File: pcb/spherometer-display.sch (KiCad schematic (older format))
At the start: 12 parts, among them J1 Battery, J2 Indicator, J3 Display, Q1 NPN, Q2 NPN, SW1 SmallPush, SW2 LargePush, U1 ATTINY85V-10SU

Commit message: Adapt to Kicad 5.1 symbols.
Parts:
- removed J3: Display, Pin_Headers:Pin_Header_Straight_1x04_Pitch2.54mm, symbol Connector:Conn_01x04
- removed SW1: SmallPush, Buttons_Switches_SMD:SW_SPST_PTS645, symbol Switch:SW_Push
- added J3: Display, Connector_PinHeader_2.54mm:PinHeader_1x04_P2.54mm_Vertical, symbol Connector_Generic:Conn_01x04
- C1: footprint Capacitors_SMD:C_0603 -> Capacitor_SMD:C_0603_1608Metric; symbol device:C -> Device:C
- J1: footprint Connectors_JST:JST_PH_S3B-PH-K_03x2.00mm_Angled -> Connector_JST:JST_PH_S3B-PH-K_1x03_P2.00mm_Horizontal; symbol Connector:Conn_01x03 -> Connector_Generic:Conn_01x03
- J2: footprint Connectors_JST:JST_PH_S4B-PH-K_04x2.00mm_Angled -> Connector_JST:JST_PH_S4B-PH-K_1x04_P2.00mm_Horizontal; symbol Connector:Conn_01x04 -> Connector_Generic:Conn_01x04
- Q1, Q2: footprint TO_SOT_Packages_SMD:SOT-23 -> Package_TO_SOT_SMD:SOT-23; symbol device:Q_NPN_BEC -> Device:Q_NPN_BEC
- R1, R2, R3: footprint Resistors_SMD:R_0603 -> Resistor_SMD:R_0603_1608Metric; symbol device:R -> Device:R
- SW2: value LargePush -> UI-Button; footprint Buttons_Switches_SMD:SW_SPST_TL3342 -> Button_Switch_THT:SW_Tactile_SPST_Angled_PTS645Vx83-2LFS
- U1: footprint Housings_SOIC:SOIC-8_3.9x4.9mm_Pitch1.27mm -> Package_SO:SOIC-8_3.9x4.9mm_P1.27mm; symbol atmel:ATTINY85-20SU -> MCU_Microchip_ATtiny:ATtiny85V-10SU
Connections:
- net GND: now also J3.3 (Pin_3)
- net SCL: now also J3.2 (Pin_2)
- net SDA: now also J3.1 (Pin_1)
- net VCC: now also J3.4 (Pin_4)
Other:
- note removed: "Alternatives"
- moved on the sheet: C1, R3, U1
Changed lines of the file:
@@
 $EndDescr
 $Comp
-L device:Q_NPN_BEC Q2
+L Device:Q_NPN_BEC Q2
 U 1 1 5C7BA6FA
 P 2750 4050
 F 0 "Q2" H 2941 4096 50  0000 L CNN
 F 1 "NPN" H 2941 4005 50  0000 L CNN
-F 2 "TO_SOT_Packages_SMD:SOT-23" H 2950 4150 50  0001 C CNN
+F 2 "Package_TO_SOT_SMD:SOT-23" H 2950 4150 50  0001 C CNN
 F 3 "" H 2750 4050 50  0001 C CNN
 	1    2750 4050
@@
 L power:VCC #PWR0103
 U 1 1 5C7BC608
-P 6100 2900
-F 0 "#PWR0103" H 6100 2750 50  0001 C CNN
-F 1 "VCC" H 6117 3073 50  0000 C CNN
-F 2 "" H 6100 2900 50  0001 C CNN
-F 3 "" H 6100 2900 50  0001 C CNN
-	1    6100 2900
+P 4950 2600
+F 0 "#PWR0103" H 4950 2450 50  0001 C CNN
+F 1 "VCC" H 4967 2773 50  0000 C CNN
+F 2 "" H 4950 2600 50  0001 C CNN
+F 3 "" H 4950 2600 50  0001 C CNN
+	1    4950 2600
 	1    0    0    -1
 $EndComp
@@
 L power:GND #PWR0104
 U 1 1 5C7BCED2
-P 6100 3400
-F 0 "#PWR0104" H 6100 3150 50  0001 C CNN
-F 1 "GND" H 6105 3227 50  0000 C CNN
-F 2 "" H 6100 3400 50  0001 C CNN
-F 3 "" H 6100 3400 50  0001 C CNN
-	1    6100 3400
-	1    0    0    -1
-$EndComp
-$Comp
-L Connector:Conn_01x04 J3
-U 1 1 5C7BD895
-P 2750 2200
-F 0 "J3" V 2714 1912 50  0000 R CNN
-F 1 "Display" V 2623 1912 50  0000 R CNN
-F 2 "Pin_Headers:Pin_Header_Straight_1x04_Pitch2.54mm" H 2750 2200 50  0001 C CNN
-F 3 "~" H 2750 2200 50  0001 C CNN
-	1    2750 2200
-	0    -1   -1   0
+P 4950 3800
+F 0 "#PWR0104" H 4950 3550 50  0001 C CNN
+F 1 "GND" H 4955 3627 50  0000 C CNN
+F 2 "" H 4950 3800 50  0001 C CNN
+F 3 "" H 4950 3800 50  0001 C CNN
+	1    4950 3800
+	1    0    0    -1
 $EndComp
 $Comp
@@
 $EndComp
 $Comp
-L atmel:ATTINY85-20SU U1
+L MCU_Microchip_ATtiny:ATtiny85V-10SU U1
 U 1 1 5C7C0CD1
-P 4750 3150
-F 0 "U1" H 4750 3667 50  0000 C CNN
-F 1 "ATTINY85V-10SU" H 4750 3576 50  0000 C CNN
-F 2 "Housings_SOIC:SOIC-8_3.9x4.9mm_Pitch1.27mm" H 5700 3150 50  0001 C CIN
-F 3 "http://www.atmel.com/images/atmel-2586-avr-8-bit-microcontroller-attiny25-attiny45-attiny85_datasheet.pdf" H 4750 3150 50  0001 C CNN
-	1    4750 3150
-	1    0    0    -1
+P 4050 3200
+F 0 "U1" H 3650 3450 50  0000 C CNN
+F 1 "ATTINY85V-10SU" H 3900 3350 50  0000 C CNN
+F 2 "Package_SO:SOIC-8_3.9x4.9mm_P1.27mm" H 5000 3200 50  0001 C CIN
+F 3 "http://www.atmel.com/images/atmel-2586-avr-8-bit-microcontroller-attiny25-attiny45-attiny85_datasheet.pdf" H 4050 3200 50  0001 C CNN
+	1    4050 3200
+	-1   0    0    -1
 $EndComp
 Wire Wire Line
 	2650 2400 2650 2900
 Wire Wire Line
-	2650 2900 3400 2900
+	2650 2900 3450 2900
 Wire Wire Line
 	2750 2400 2750 3100
 Wire Wire Line
-	2750 3100 3400 3100
+	2750 3100 3450 3100
 Text Label 2900 2900 0    50   ~ 0
 SDA
@@
 P 3750 2400
 F 0 "SW2" H 4250 2500 50  0000 C CNN
-F 1 "LargePush" H 4250 2400 50  0000 C CNN
-F 2 "Buttons_Switches_SMD:SW_SPST_TL3342" H 3750 2600 50  0001 C CNN
+F 1 "UI-Button" H 4250 2400 50  0000 C CNN
+F 2 "Button_Switch_THT:SW_Tactile_SPST_Angled_PTS645Vx83-2LFS" H 3750 2600 50  0001 C CNN
 F 3 "" H 3750 2600 50  0001 C CNN
 	1    3750 2400
@@
 	3300 2400 3300 3000
 Wire Wire Line
-	3300 3000 3400 3000
+	3300 3000 3450 3000
 Text Label 3300 2600 0    50   ~ 0
 Button
 Wire Wire Line
-	2850 3200 3400 3200
+	2850 3200 3450 3200
 Wire Wire Line
 	2850 3850 3200 3850
@@
 	3200 3850 3200 3300
 Wire Wire Line
-	3200 3300 3400 3300
-$Comp
-L device:Q_NPN_BEC Q1
+	3200 3300 3450 3300
+$Comp
+L Device:Q_NPN_BEC Q1
 U 1 1 5C7C80D0
 P 2750 3400
 F 0 "Q1" H 2941 3446 50  0000 L CNN
 F 1 "NPN" H 2941 3355 50  0000 L CNN
-F 2 "TO_SOT_Packages_SMD:SOT-23" H 2950 3500 50  0001 C CNN
+F 2 "Package_TO_SOT_SMD:SOT-23" H 2950 3500 50  0001 C CNN
 F 3 "" H 2750 3400 50  0001 C CNN
 	1    2750 3400
@@
 $EndComp
 $Comp
-L Connector:Conn_01x04 J2
+L Connector_Generic:Conn_01x04 J2
 U 1 1 5C7C8F49
 P 2050 2200
-F 0 "J2" V 2014 1912 50  0000 R CNN
+F 0 "J2" V 2050 2450 50  0000 R CNN
 F 1 "Indicator" V 1950 2700 50  0000 R CNN
-F 2 "Connectors_JST:JST_PH_S4B-PH-K_04x2.00mm_Angled" H 2050 2200 50  0001 C CNN
+F 2 "Connector_JST:JST_PH_S4B-PH-K_1x04_P2.00mm_Horizontal" H 2050 2200 50  0001 C CNN
 F 3 "~" H 2050 2200 50  0001 C CNN
 	1    2050 2200
@@
 $EndComp
 $Comp
-L device:R R1
+L Device:R R1
 U 1 1 5C7CA7C5
 P 2400 3400
 F 0 "R1" V 2193 3400 50  0000 C CNN
 F 1 "33k" V 2284 3400 50  0000 C CNN
-F 2 "Resistors_SMD:R_0603" V 2330 3400 50  0001 C CNN
+F 2 "Resistor_SMD:R_0603_1608Metric" V 2330 3400 50  0001 C CNN
 F 3 "" H 2400 3400 50  0001 C CNN
 	1    2400 3400
@@
 $EndComp
 $Comp
-L device:R R2
+L Device:R R2
 U 1 1 5C7CB12C
 P 2400 4050
 F 0 "R2" V 2193 4050 50  0000 C CNN
 F 1 "33k" V 2284 4050 50  0000 C CNN
-F 2 "Resistors_SMD:R_0603" V 2330 4050 50  0001 C CNN
+F 2 "Resistor_SMD:R_0603_1608Metric" V 2330 4050 50  0001 C CNN
 F 3 "" H 2400 4050 50  0001 C CNN
 	1    2400 4050
@@
 	2050 4050 2250 4050
 $Comp
-L Connector:Conn_01x03 J1
+L Connector_Generic:Conn_01x03 J1
 U 1 1 5C7CC029
 P 1300 3050
 F 0 "J1" H 1300 2850 50  0000 C CNN
 F 1 "Battery" H 1500 3050 50  0000 C CNN
-F 2 "Connectors_JST:JST_PH_S3B-PH-K_03x2.00mm_Angled" H 1300 3050 50  0001 C CNN
+F 2 "Connector_JST:JST_PH_S3B-PH-K_1x03_P2.00mm_Horizontal" H 1300 3050 50  0001 C CNN
 F 3 "~" H 1300 3050 50  0001 C CNN
 	1    1300 3050
@@
 $EndComp
 $Comp
-L Switch:SW_Push SW1
-U 1 1 5C7D1A93
-P 3750 2200
-F 0 "SW1" H 4200 2300 50  0000 C CNN
-F 1 "SmallPush" H 4250 2200 50  0000 C CNN
-F 2 "Buttons_Switches_SMD:SW_SPST_PTS645" H 3750 2400 50  0001 C CNN
-F 3 "" H 3750 2400 50  0001 C CNN
-	1    3750 2200
-	1    0    0    -1
-$EndComp
-Wire Wire Line
-	3550 2200 3550 2400
-Connection ~ 3550 2400
-Wire Wire Line
-	3950 2200 3950 2400
-Connection ~ 3950 2400
-Text Notes 4500 2350 0    50   ~ 0
-Alternatives
-$Comp
-L device:R R3
+L Device:R R3
 U 1 1 5C7D3C7F
-P 3400 3550
-F 0 "R3" H 3330 3504 50  0000 R CNN
-F 1 "33k" H 3330 3595 50  0000 R CNN
-F 2 "Resistors_SMD:R_0603" V 3330 3550 50  0001 C CNN
-F 3 "" H 3400 3550 50  0001 C CNN
-	1    3400 3550
+P 3350 3550
+F 0 "R3" H 3300 3700 50  0000 R CNN
+F 1 "33k" V 3350 3650 50  0000 R CNN
+F 2 "Resistor_SMD:R_0603_1608Metric" V 3280 3550 50  0001 C CNN
+F 3 "" H 3350 3550 50  0001 C CNN
+	1    3350 3550
 	-1   0    0    1
 $EndComp
@@
 L power:VCC #PWR01
 U 1 1 5C7D4897
-P 3400 3700
-F 0 "#PWR01" H 3400 3550 50  0001 C CNN
-F 1 "VCC" V 3417 3828 50  0000 L CNN
-F 2 "" H 3400 3700 50  0001 C CNN
-F 3 "" H 3400 3700 50  0001 C CNN
-	1    3400 3700
-	0    1    1    0
-$EndComp
-$Comp
-L device:C C1
+P 3350 3700
+F 0 "#PWR01" H 3350 3550 50  0001 C CNN
+F 1 "VCC" V 3367 3828 50  0000 L CNN
+F 2 "" H 3350 3700 50  0001 C CNN
+F 3 "" H 3350 3700 50  0001 C CNN
+	1    3350 3700
+	-1   0    0    1
+$EndComp
+$Comp
+L Device:C C1
 U 1 1 5C7B9330
-P 6100 3150
-F 0 "C1" H 6215 3196 50  0000 L CNN
-F 1 "100n" H 6215 3105 50  0000 L CNN
-F 2 "Capacitors_SMD:C_0603" H 6138 3000 50  0001 C CNN
-F 3 "" H 6100 3150 50  0001 C CNN
-	1    6100 3150
-	1    0    0    -1
-$EndComp
-Wire Wire Line
-	6100 2900 6100 3000
-Connection ~ 6100 2900
-Wire Wire Line
-	6100 3300 6100 3400
-Connection ~ 6100 3400
+P 4950 3200
+F 0 "C1" H 5065 3246 50  0000 L CNN
+F 1 "100n" H 5065 3155 50  0000 L CNN
+F 2 "Capacitor_SMD:C_0603_1608Metric" H 4988 3050 50  0001 C CNN
+F 3 "" H 4950 3200 50  0001 C CNN
+	1    4950 3200
+	1    0    0    -1
+$EndComp
+$Comp
+L Connector_Generic:Conn_01x04 J3
+U 1 1 5CBCFE92
+P 2750 2200
+F 0 "J3" V 2714 1912 50  0000 R CNN
+F 1 "Display" V 2650 1950 50  0000 R CNN
+F 2 "Connector_PinHeader_2.54mm:PinHeader_1x04_P2.54mm_Vertical" H 2750 2200 50  0001 C CNN
+F 3 "~" H 2750 2200 50  0001 C CNN
+	1    2750 2200
+	0    -1   -1   0
+$EndComp
+Wire Wire Line
+	3450 3400 3350 3400
+Wire Wire Line
+	4050 3800 4950 3800
+Wire Wire Line
+	4950 3350 4950 3800
+Connection ~ 4950 3800
+Wire Wire Line
+	4050 2600 4950 2600
+Wire Wire Line
+	4950 2600 4950 3050
+Connection ~ 4950 2600
 $EndSCHEMATC

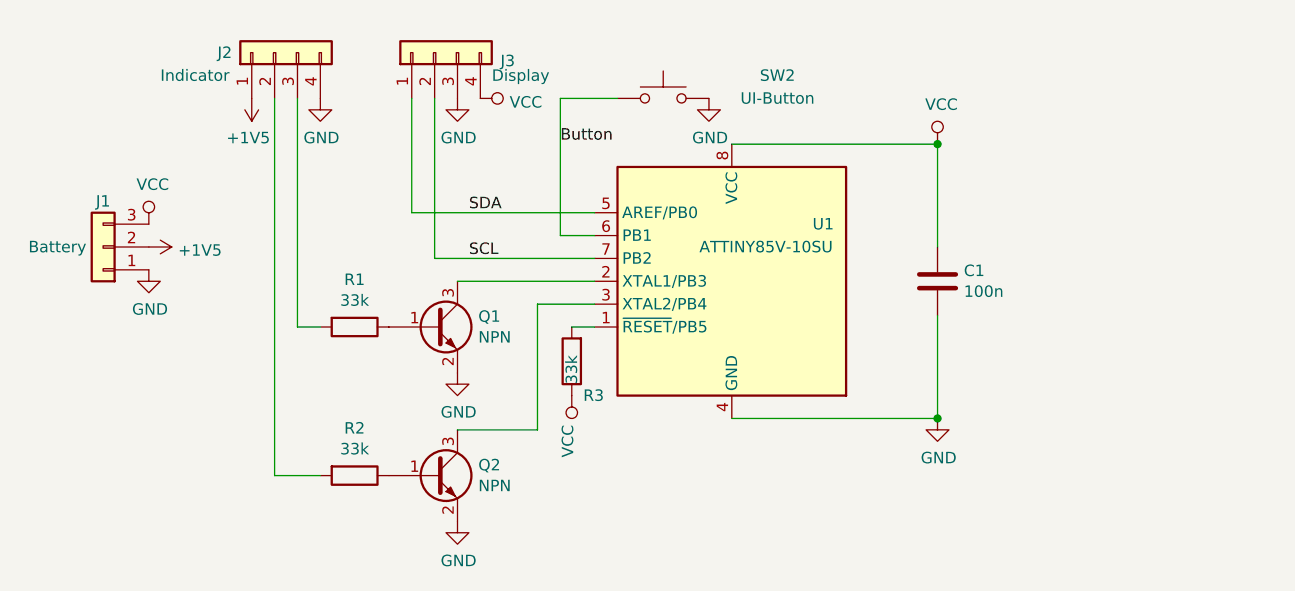
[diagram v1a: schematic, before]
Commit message: Prepare to be usable with dial indicators that already provide OpenCollector output.
Add a solder-jumper that allows to directly wire the indicator directly to Attiny.
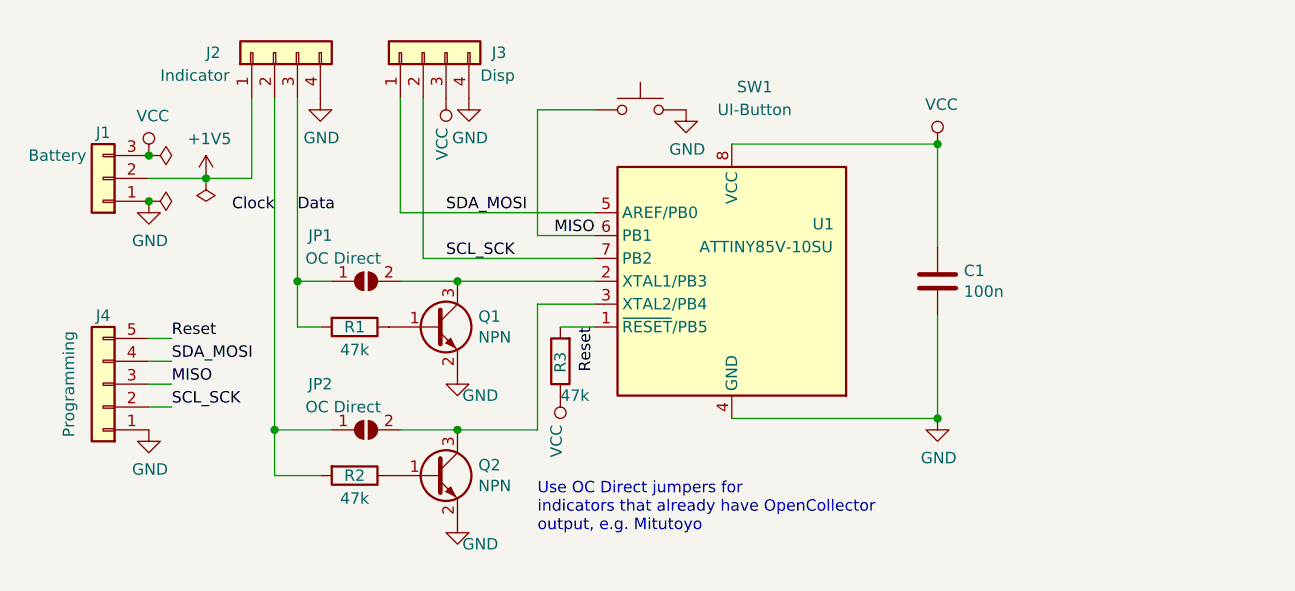
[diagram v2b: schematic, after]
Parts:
- added J4: Programming, Connector_PinHeader_2.54mm:PinHeader_1x05_P2.54mm_Vertical, symbol Connector_Generic:Conn_01x05
- added JP1, JP2: OC Direct, Jumper:SolderJumper-2_P1.3mm_Open_RoundedPad1.0x1.5mm, symbol Jumper:SolderJumper_2_Open
- J3: value Display -> Disp
- R1, R2, R3: value 33k -> 47k
- SW1: renamed from SW2; footprint Button_Switch_THT:SW_Tactile_SPST_Angled_PTS645Vx83-2LFS -> digi-spherometer:EVPAV-Switch
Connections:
- net GND: now also J3.4 (Pin_4), J4.1 (Pin_1); no longer J3.3 (Pin_3)
- net VCC: now also J3.3 (Pin_3); no longer J3.4 (Pin_4)
- net at Q2.3 (C), U1.3 (XTAL2/PB4): now also JP2.2 (B)
- net Reset: now reaches R3.2, U1.1 (~RESET~/PB5)
- net Reset: now also J4.5 (Pin_5)
- net at Q1.3 (C), U1.2 (XTAL1/PB3): now also JP1.2 (B)
- net Clock: now reaches J2.2 (Pin_2), R2.2
- net Clock: now also JP2.1 (A)
- net Data: now reaches J2.3 (Pin_3), R1.2
- net Data: now also JP1.1 (A)
- net Button renamed MISO
- net MISO: now also J4.3 (Pin_3)
- net SCL renamed SCL_SCK
- net SCL_SCK: now also J4.2 (Pin_2)
- net SDA renamed SDA_MOSI
- net SDA_MOSI: now also J4.4 (Pin_4)
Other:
- note added: "Use OC Direct jumpers for\nindicators that already have OpenCollector\noutput, e.g. Mitutoyo"
- moved on the sheet: J1, J3, R3, SW1

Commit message: Route board; add Makefile to create fab files.
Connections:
- net GND: now also SW1.1; no longer SW1.2
- net MISO: now also SW1.2; no longer SW1.1
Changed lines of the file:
@@
 U 1 1 5C7C2518
 P 3650 2450
-F 0 "SW1" H 4150 2550 50  0000 C CNN
-F 1 "UI-Button" H 4150 2450 50  0000 C CNN
+F 0 "SW1" H 3450 2600 50  0000 C CNN
+F 1 "UI-Button" H 3300 2500 50  0000 C CNN
 F 2 "digi-spherometer:EVPAV-Switch" H 3650 2650 50  0001 C CNN
 F 3 "" H 3650 2650 50  0001 C CNN
 	1    3650 2450
-	1    0    0    -1
+	-1   0    0    -1
 $EndComp
 $Comp

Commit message: Swap pin sequence of indicator connector.
With a flat cable from the autolet indicator, the GND pin is towards
the center.
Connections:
- net +1V5: now also J2.4 (Pin_4); no longer J2.1 (Pin_1)
- net Clock: now also J2.3 (Pin_3), JP1.1 (A), R1.2; no longer J2.2 (Pin_2), JP2.1 (A), R2.2
- net Data: now also J2.2 (Pin_2), JP2.1 (A), R2.2; no longer J2.3 (Pin_3), JP1.1 (A), R1.2
- net GND: now also J2.1 (Pin_1), J3.1 (Pin_1); no longer J2.4 (Pin_4), J3.4 (Pin_4)
- net SCL_SCK: now also J3.3 (Pin_3); no longer J3.2 (Pin_2)
- net SDA_MOSI: now also J3.4 (Pin_4); no longer J3.1 (Pin_1)
- net VCC: now also J3.2 (Pin_2); no longer J3.3 (Pin_3)
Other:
- note added: "Use OC Direct jumpers for\nindicators that already have OpenCollector\noutput, e.g. Mitutoyo\nThen R1, R2, Q1, Q2 are not needed."
- note removed: "Use OC Direct jumpers for\nindicators that already have OpenCollector\noutput, e.g. Mitutoyo"
- moved on the sheet: JP1, JP2, Q1, Q2, R1, R2
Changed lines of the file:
@@
 L Device:Q_NPN_BEC Q2
 U 1 1 5C7BA6FA
-P 2750 4050
-F 0 "Q2" H 2941 4096 50  0000 L CNN
-F 1 "NPN" H 2941 4005 50  0000 L CNN
-F 2 "Package_TO_SOT_SMD:SOT-23" H 2950 4150 50  0001 C CNN
-F 3 "" H 2750 4050 50  0001 C CNN
-	1    2750 4050
+P 2750 3400
+F 0 "Q2" H 2941 3446 50  0000 L CNN
+F 1 "NPN" H 2941 3355 50  0000 L CNN
+F 2 "Package_TO_SOT_SMD:SOT-23" H 2950 3500 50  0001 C CNN
+F 3 "" H 2750 3400 50  0001 C CNN
+	1    2750 3400
 	1    0    0    -1
 $EndComp
@@
 $EndComp
 Wire Wire Line
-	2850 3200 3450 3200
-Wire Wire Line
 	2850 3850 3200 3850
-Wire Wire Line
-	3200 3850 3200 3300
-Wire Wire Line
-	3200 3300 3450 3300
 $Comp
 L Device:Q_NPN_BEC Q1
 U 1 1 5C7C80D0
-P 2750 3400
-F 0 "Q1" H 2941 3446 50  0000 L CNN
-F 1 "NPN" H 2941 3355 50  0000 L CNN
-F 2 "Package_TO_SOT_SMD:SOT-23" H 2950 3500 50  0001 C CNN
-F 3 "" H 2750 3400 50  0001 C CNN
-	1    2750 3400
+P 2750 4050
+F 0 "Q1" H 2941 4096 50  0000 L CNN
+F 1 "NPN" H 2941 4005 50  0000 L CNN
+F 2 "Package_TO_SOT_SMD:SOT-23" H 2950 4150 50  0001 C CNN
+F 3 "" H 2750 4050 50  0001 C CNN
+	1    2750 4050
 	1    0    0    -1
 $EndComp
@@
 L Connector_Generic:Conn_01x04 J2
 U 1 1 5C7C8F49
-P 2050 2200
-F 0 "J2" V 2050 2500 50  0000 R CNN
-F 1 "Indicator" V 1950 2700 50  0000 R CNN
-F 2 "Connector_JST:JST_PH_S4B-PH-K_1x04_P2.00mm_Horizontal" H 2050 2200 50  0001 C CNN
-F 3 "~" H 2050 2200 50  0001 C CNN
-	1    2050 2200
-	0    -1   -1   0
+P 2150 2200
+F 0 "J2" V 2150 1900 50  0000 R CNN
+F 1 "Indicator" V 2050 1900 50  0000 R CNN
+F 2 "Connector_JST:JST_PH_S4B-PH-K_1x04_P2.00mm_Horizontal" H 2150 2200 50  0001 C CNN
+F 3 "~" H 2150 2200 50  0001 C CNN
+	1    2150 2200
+	0    1    -1   0
 $EndComp
 $Comp
@@
 L Device:R R1
 U 1 1 5C7CA7C5
+P 2400 4050
+F 0 "R1" V 2400 4050 50  0000 C CNN
+F 1 "47k" V 2500 4050 50  0000 C CNN
+F 2 "Resistor_SMD:R_0603_1608Metric" V 2330 4050 50  0001 C CNN
+F 3 "" H 2400 4050 50  0001 C CNN
+	1    2400 4050
+	0    1    1    0
+$EndComp
+$Comp
+L Device:R R2
+U 1 1 5C7CB12C
 P 2400 3400
-F 0 "R1" V 2400 3400 50  0000 C CNN
+F 0 "R2" V 2400 3400 50  0000 C CNN
 F 1 "47k" V 2500 3400 50  0000 C CNN
 F 2 "Resistor_SMD:R_0603_1608Metric" V 2330 3400 50  0001 C CNN
 F 3 "" H 2400 3400 50  0001 C CNN
 	1    2400 3400
-	0    1    1    0
-$EndComp
-$Comp
-L Device:R R2
-U 1 1 5C7CB12C
-P 2400 4050
-F 0 "R2" V 2400 4050 50  0000 C CNN
-F 1 "47k" V 2500 4050 50  0000 C CNN
-F 2 "Resistor_SMD:R_0603_1608Metric" V 2330 4050 50  0001 C CNN
-F 3 "" H 2400 4050 50  0001 C CNN
-	1    2400 4050
 	0    1    1    0
 $EndComp
@@
 L Connector_Generic:Conn_01x04 J3
 U 1 1 5CBCFE92
-P 2700 2200
-F 0 "J3" V 2700 1900 50  0000 R CNN
-F 1 "Disp" V 2600 1950 50  0000 R CNN
-F 2 "Connector_PinHeader_2.54mm:PinHeader_1x04_P2.54mm_Vertical" H 2700 2200 50  0001 C CNN
-F 3 "~" H 2700 2200 50  0001 C CNN
-	1    2700 2200
-	0    -1   -1   0
+P 2800 2200
+F 0 "J3" V 2800 2500 50  0000 R CNN
+F 1 "Disp" V 2700 2550 50  0000 R CNN
+F 2 "Connector_PinHeader_2.54mm:PinHeader_1x04_P2.54mm_Vertical" H 2800 2200 50  0001 C CNN
+F 3 "~" H 2800 2200 50  0001 C CNN
+	1    2800 2200
+	0    1    -1   0
 $EndComp
 Wire Wire Line
@@
 L Jumper:SolderJumper_2_Open JP1
 U 1 1 5CC4FCB3
+P 2450 3850
+F 0 "JP1" H 2250 4050 50  0000 C CNN
+F 1 "OC Direct" H 2350 3950 50  0000 C CNN
+F 2 "Jumper:SolderJumper-2_P1.3mm_Open_RoundedPad1.0x1.5mm" H 2450 3850 50  0001 C CNN
+F 3 "~" H 2450 3850 50  0001 C CNN
+	1    2450 3850
+	1    0    0    -1
+$EndComp
+Wire Wire Line
+	2150 3200 2300 3200
+Connection ~ 2150 3200
+Wire Wire Line
+	2150 3200 2150 3400
+Wire Wire Line
+	2600 3200 2850 3200
+$Comp
+L Jumper:SolderJumper_2_Open JP2
+U 1 1 5CC51175
 P 2450 3200
-F 0 "JP1" H 2250 3400 50  0000 C CNN
+F 0 "JP2" H 2250 3400 50  0000 C CNN
 F 1 "OC Direct" H 2350 3300 50  0000 C CNN
 F 2 "Jumper:SolderJumper-2_P1.3mm_Open_RoundedPad1.0x1.5mm" H 2450 3200 50  0001 C CNN
 F 3 "~" H 2450 3200 50  0001 C CNN
 	1    2450 3200
-	1    0    0    -1
-$EndComp
-Wire Wire Line
-	2150 3200 2300 3200
-Connection ~ 2150 3200
-Wire Wire Line
-	2150 3200 2150 3400
-Wire Wire Line
-	2600 3200 2850 3200
-Connection ~ 2850 3200
-$Comp
-L Jumper:SolderJumper_2_Open JP2
-U 1 1 5CC51175
-P 2450 3850
-F 0 "JP2" H 2250 4050 50  0000 C CNN
-F 1 "OC Direct" H 2350 3950 50  0000 C CNN
-F 2 "Jumper:SolderJumper-2_P1.3mm_Open_RoundedPad1.0x1.5mm" H 2450 3850 50  0001 C CNN
-F 3 "~" H 2450 3850 50  0001 C CNN
-	1    2450 3850
 	1    0    0    -1
 $EndComp
@@
 Wire Wire Line
 	3200 3000 3450 3000
-Text Notes 3200 4300 0    50   ~ 0
-Use OC Direct jumpers for\nindicators that already have OpenCollector\noutput, e.g. Mitutoyo
+Text Notes 3200 4350 0    50   ~ 0
+Use OC Direct jumpers for\nindicators that already have OpenCollector\noutput, e.g. Mitutoyo\nThen R1, R2, Q1, Q2 are not needed.
 $Comp
 L power:PWR_FLAG #FLG0101
@@
 Text Label 2050 2900 2    50   ~ 0
 Clock
+Wire Wire Line
+	2850 3200 3100 3200
+Wire Wire Line
+	3100 3200 3100 3300
+Wire Wire Line
+	3100 3300 3450 3300
+Connection ~ 2850 3200
+Wire Wire Line
+	3200 3850 3200 3200
+Wire Wire Line
+	3200 3200 3450 3200
 $EndSCHEMATC

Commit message: Fix: Attiny85 is the huge 5.3mm SOIC-8 footprint.
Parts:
- U1: footprint Package_SO:SOIC-8_3.9x4.9mm_P1.27mm -> Package_SO:SOIC-8_5.23x5.23mm_P1.27mm
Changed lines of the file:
@@
 F 0 "U1" H 3650 3450 50  0000 C CNN
 F 1 "ATTINY85V-10SU" H 3900 3350 50  0000 C CNN
-F 2 "Package_SO:SOIC-8_3.9x4.9mm_P1.27mm" H 5000 3200 50  0001 C CIN
+F 2 "Package_SO:SOIC-8_5.23x5.23mm_P1.27mm" H 5000 3200 50  0001 C CIN
 F 3 "http://www.atmel.com/images/atmel-2586-avr-8-bit-microcontroller-attiny25-attiny45-attiny85_datasheet.pdf" H 4050 3200 50  0001 C CNN
 	1    4050 3200
